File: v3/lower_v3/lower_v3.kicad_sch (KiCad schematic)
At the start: 12 parts, among them J1 To Power Bank, J10 PIN_RING_MOTOR, J11 PIN_PINKY_MOTOR, J2 PIN_PINKY, J3 PIN_RING, J4 PIN_MIDDLE, J5 PIN_INDEX, J6 PIN_THUMB, J7 PIN_THUMB_MOTOR, J8 PIN_INDEX_MOTOR, J9 PIN_MIDDLE_MOTOR, U1 ESP32-DEVKIT-V1

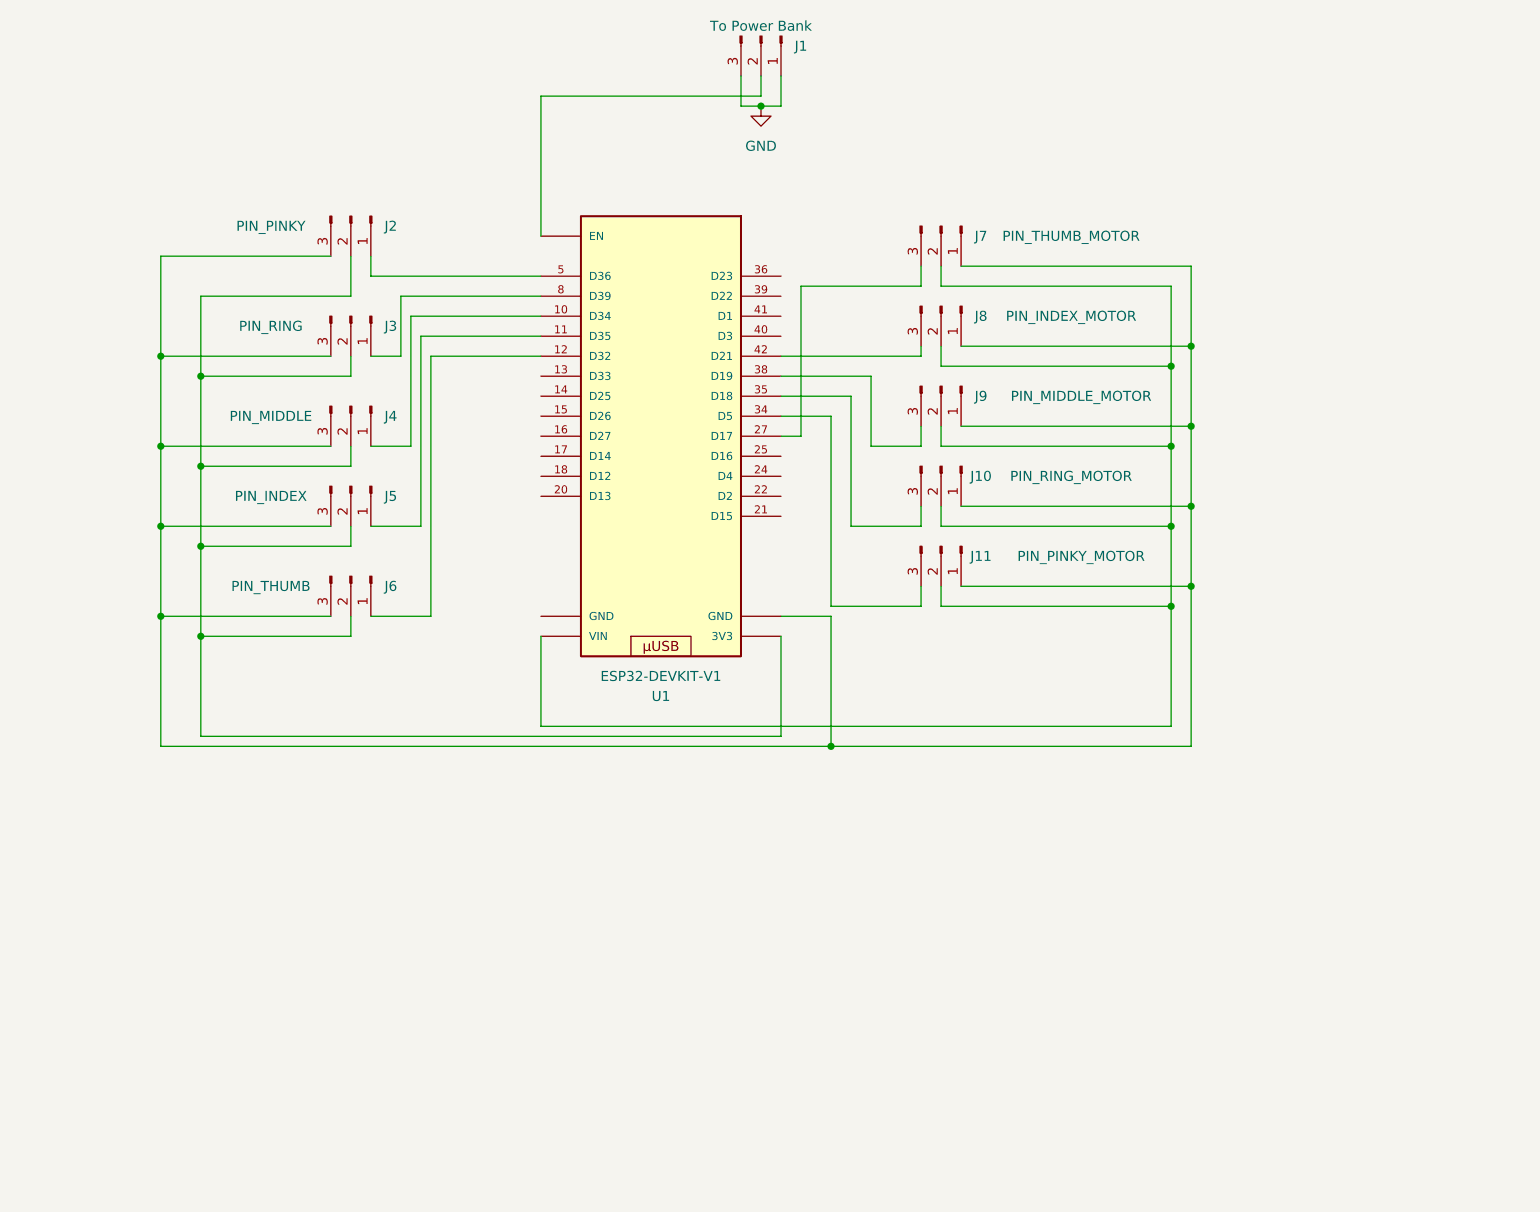
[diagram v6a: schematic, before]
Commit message: Add more pins
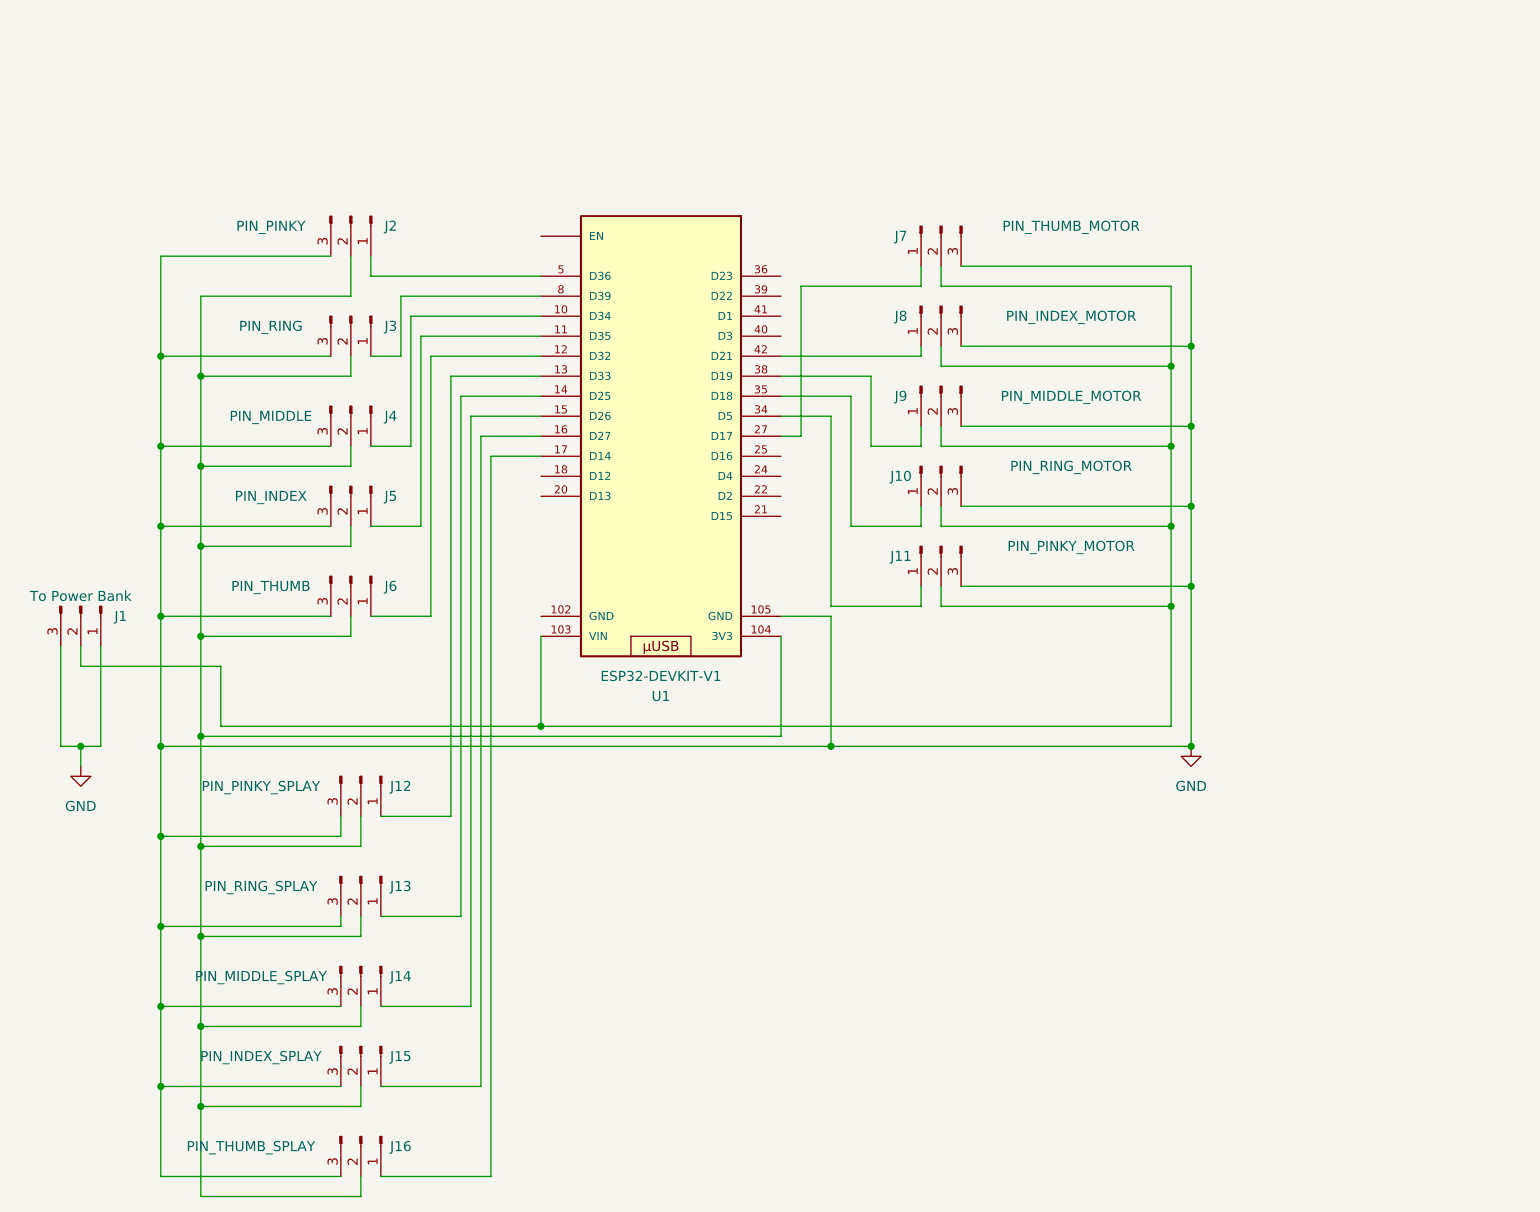
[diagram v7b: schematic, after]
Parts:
- added J12: PIN_PINKY_SPLAY, Connector_PinHeader_2.54mm:PinHeader_1x03_P2.54mm_Vertical, symbol Connector:Conn_01x03_Male
- added J13: PIN_RING_SPLAY, Connector_PinHeader_2.54mm:PinHeader_1x03_P2.54mm_Vertical, symbol Connector:Conn_01x03_Male
- added J14: PIN_MIDDLE_SPLAY, Connector_PinHeader_2.54mm:PinHeader_1x03_P2.54mm_Vertical, symbol Connector:Conn_01x03_Male
- added J15: PIN_INDEX_SPLAY, Connector_PinHeader_2.54mm:PinHeader_1x03_P2.54mm_Vertical, symbol Connector:Conn_01x03_Male
- added J16: PIN_THUMB_SPLAY, Connector_PinHeader_2.54mm:PinHeader_1x03_P2.54mm_Vertical, symbol Connector:Conn_01x03_Male
- J1, J10, J11, J2, J3, J4, J5, J6, J7, J8, J9: footprint (none) -> Connector_PinHeader_2.54mm:PinHeader_1x03_P2.54mm_Vertical
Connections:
- net GND: now also J10.3 (Pin_3), J11.3 (Pin_3), J2.3 (Pin_3), J3.3 (Pin_3), J4.3 (Pin_3), J5.3 (Pin_3), J6.3 (Pin_3), J7.3 (Pin_3), J8.3 (Pin_3), J9.3 (Pin_3), U1.105 (GND), J12.3 (Pin_3), J13.3 (Pin_3), J14.3 (Pin_3), J15.3 (Pin_3), J16.3 (Pin_3)
- net at J2.2 (Pin_2), J3.2 (Pin_2), J4.2 (Pin_2)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: now also U1.104 (3V3), J12.2 (Pin_2), J13.2 (Pin_2), J14.2 (Pin_2), J15.2 (Pin_2), J16.2 (Pin_2); no longer U1. (VIN)
- net at J10.2 (Pin_2), J11.2 (Pin_2), J7.2 (Pin_2)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: now also J1.2 (Pin_2), U1.103 (VIN); no longer U1. (VIN)
- net at U1.34 (D5): now also J11.1 (Pin_1); no longer J11.3 (Pin_3)
- net at U1.13 (D33): now also J12.1 (Pin_1)
- net at U1.14 (D25): now also J13.1 (Pin_1)
- net at U1.15 (D26): now also J14.1 (Pin_1)
- net at U1.16 (D27): now also J15.1 (Pin_1)
- net at U1.17 (D14): now also J16.1 (Pin_1)
- net at U1.27 (D17): now also J7.1 (Pin_1); no longer J7.3 (Pin_3)
- net at U1.35 (D18): now also J10.1 (Pin_1); no longer J10.3 (Pin_3)
- net at U1.38 (D19): now also J9.1 (Pin_1); no longer J9.3 (Pin_3)
- net at U1.42 (D21): now also J8.1 (Pin_1); no longer J8.3 (Pin_3)
- now unconnected: U1. (VIN), U1. (VIN)
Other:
- moved on the sheet: J1, J10, J11, J7, J8, J9
